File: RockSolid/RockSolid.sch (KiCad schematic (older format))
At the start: 24 parts, among them Q1 IRF540N, U1 L78L05_TO92, U2 74HC04, Y1 10 Mhz

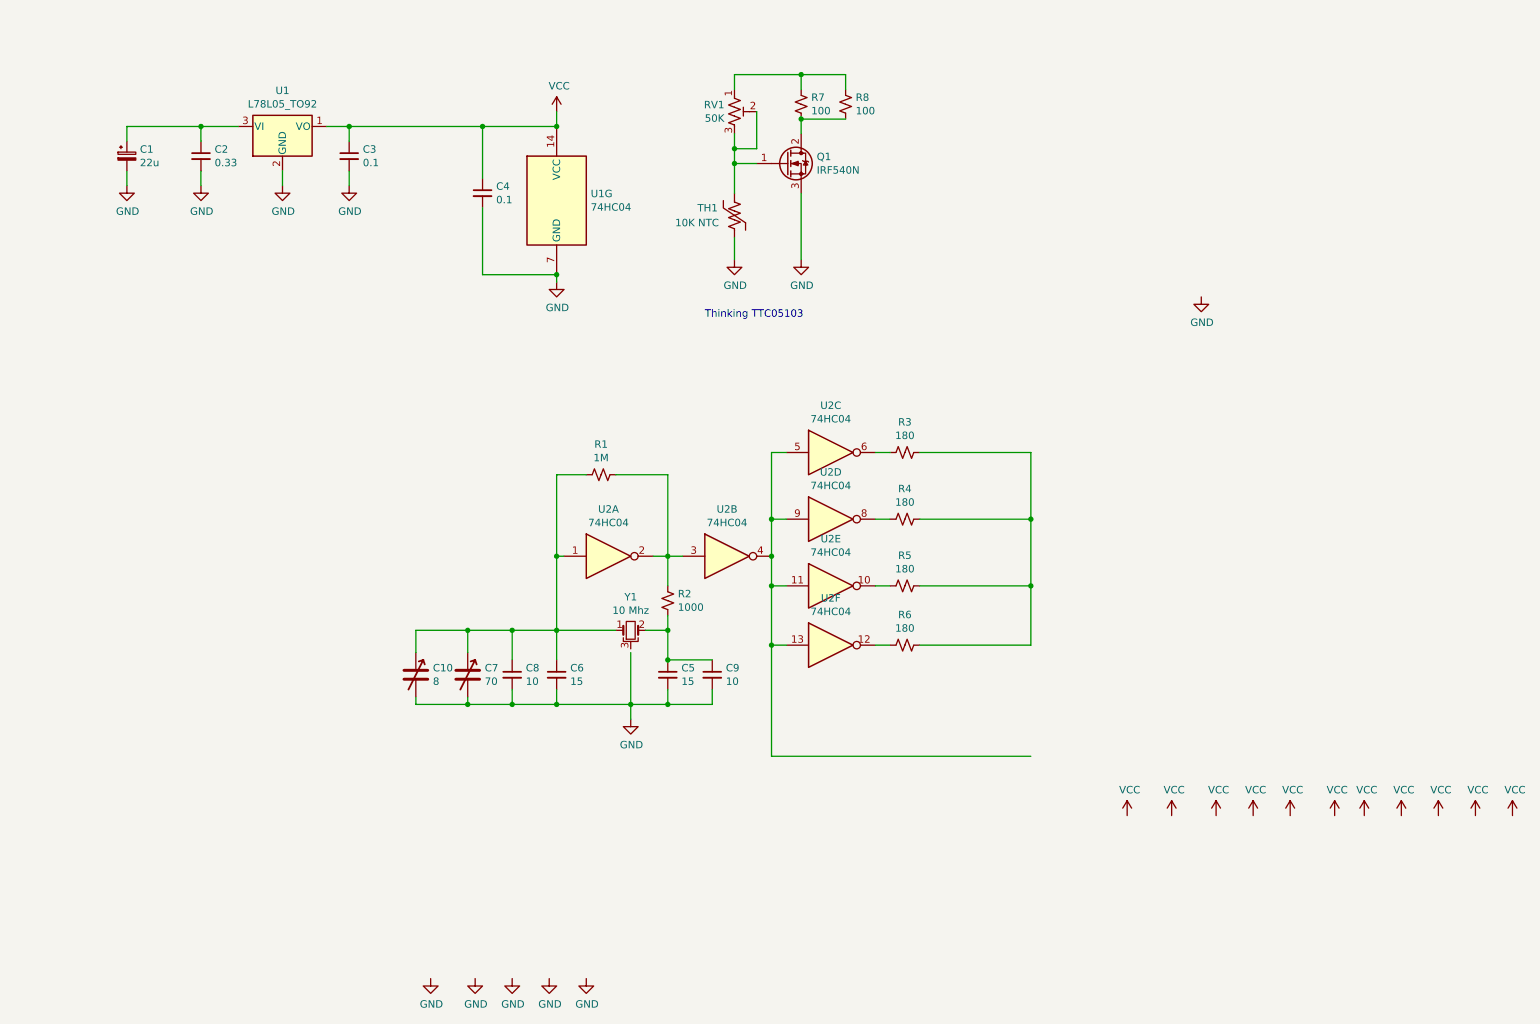
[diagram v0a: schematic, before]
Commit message: Finished schematic, initial board layout
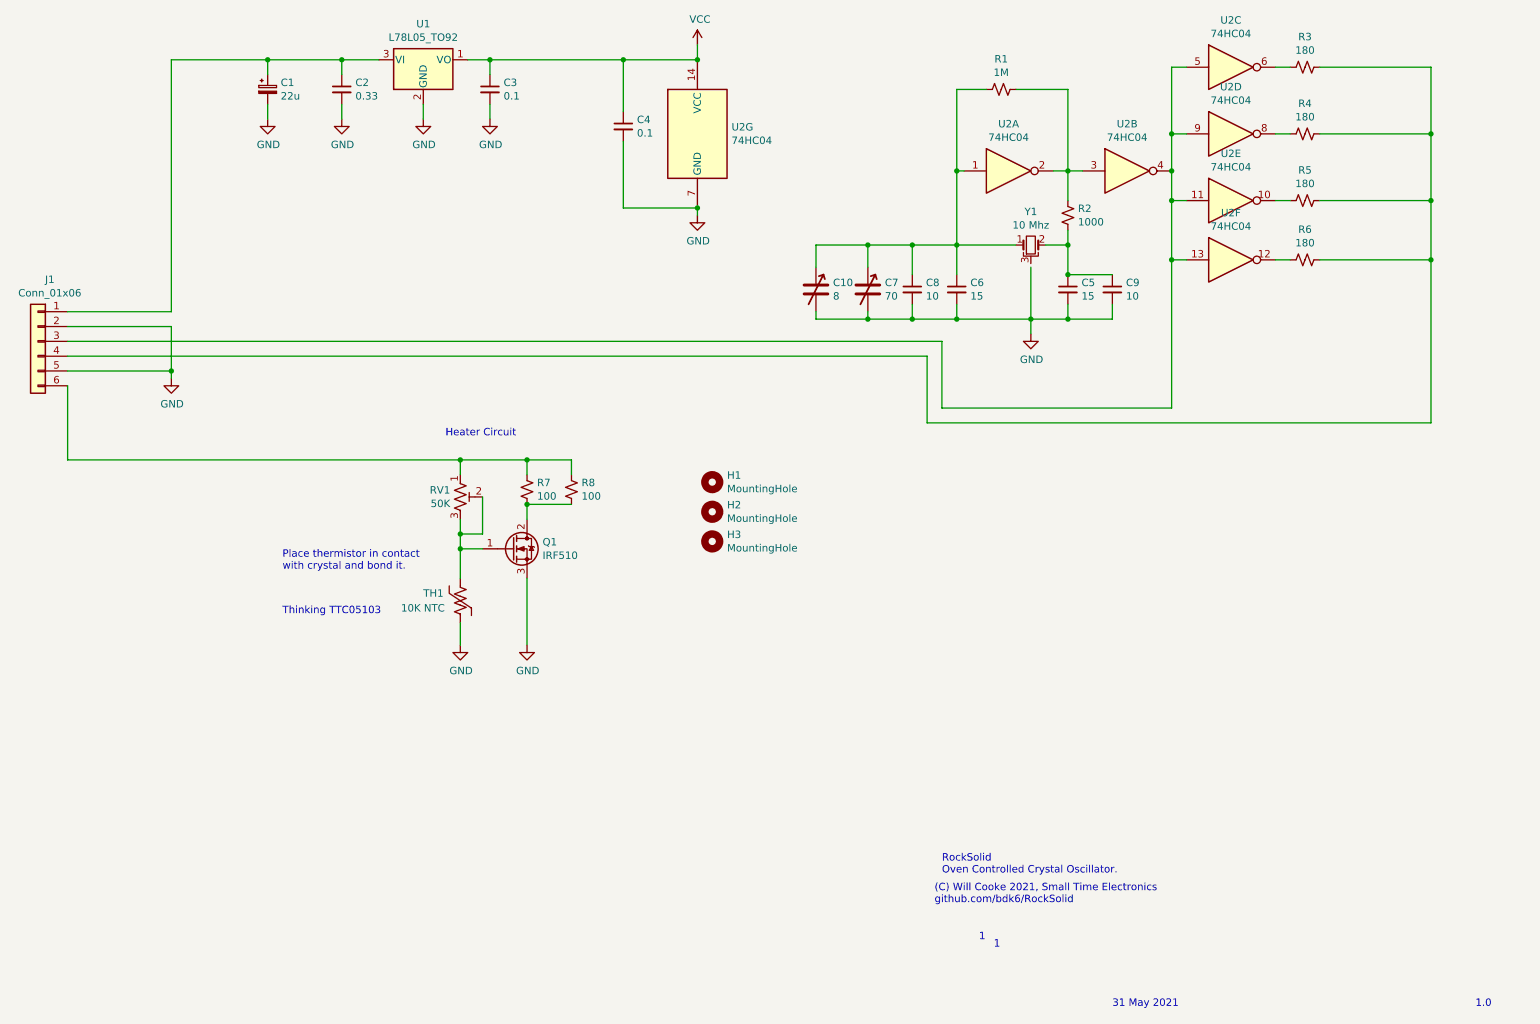
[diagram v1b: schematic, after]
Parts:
- added H1, H2, H3: MountingHole, MountingHole:MountingHole_2.5mm, symbol Mechanical:MountingHole
- added J1: Conn_01x06, Connector_PinHeader_2.54mm:PinHeader_1x06_P2.54mm_Vertical, symbol Connector_Generic:Conn_01x06
- C2, C3, C4, C5, C6, C8: footprint apacitor_THT:C_Disc_D4.7mm_W2.5mm_P5.00mm -> Capacitor_THT:C_Disc_D4.7mm_W2.5mm_P5.00mm
- Q1: value IRF540N -> IRF510
- R1, R2, R3, R4, R5, R6: footprint Resistor_THT:R_Axial_DIN0414_L11.9mm_D4.5mm_P15.24mm_Horizontal -> Resistor_THT:R_Axial_DIN0207_L6.3mm_D2.5mm_P7.62mm_Horizontal
- renumbered U1 to U2
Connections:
- net GND: now also J1.2 (Pin_2), J1.5 (Pin_5)
- net at U2.11, U2.13, U2.4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: now also J1.3 (Pin_3)
- net at R3.1, R4.1, R5.1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: now also J1.4 (Pin_4)
- net at C1.1, C2.1, U1.3 (VI): now also J1.1 (Pin_1)
- net at R7.1, R8.1, RV1.1: now also J1.6 (Pin_6)
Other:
- note added: "(C) Will Cooke 2021, Small Time Electronics\ngithub.com/bdk6/RockSolid\n"
- note added: "1"
- note added: "1.0"
- note added: "31 May 2021"
- note added: "Heater Circuit"
- note added: "Place thermistor in contact \nwith crystal and bond it."
- note added: "RockSolid \nOven Controlled Crystal Oscillator."
- moved on the sheet: C1, C10, C2, C3, C4, C5, C6, C7, C8, C9, Q1, R1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

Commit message: Version 1.0RC1 complete.
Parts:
- removed J1: Conn_01x06, Connector_PinHeader_2.54mm:PinHeader_1x06_P2.54mm_Vertical, symbol Connector_Generic:Conn_01x06
- removed R3, R4, R5, R6: 180, Resistor_THT:R_Axial_DIN0207_L6.3mm_D2.5mm_P7.62mm_Horizontal, symbol Device:R_Small_US
- added J1: Conn_01x04, Connector_PinHeader_2.54mm:PinHeader_1x04_P2.54mm_Vertical, symbol Connector_Generic:Conn_01x04
- added R10: 3K3, Resistor_THT:R_Axial_DIN0207_L6.3mm_D2.5mm_P7.62mm_Horizontal, symbol Device:R_Small_US
- added R9: 33K, Resistor_THT:R_Axial_DIN0207_L6.3mm_D2.5mm_P7.62mm_Horizontal, symbol Device:R_Small_US
- C1: footprint Capacitor_THT:CP_Radial_D8.0mm_P5.00mm -> Capacitor_THT:CP_Radial_D5.0mm_P2.00mm
- R7, R8: footprint Resistor_THT:R_Axial_DIN0414_L11.9mm_D4.5mm_P7.62mm_Vertical -> Resistor_THT:R_Axial_DIN0617_L17.0mm_D6.0mm_P7.62mm_Vertical
- RV1: value 50K -> 10K
- Y1: symbol Device:Crystal_GND3_Small -> RockSolid-rescue:Crystal_GND3_Small-Device
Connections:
- net GND: now also J1.3 (Pin_3)
- net VCC: now also R10.1
- net at U2.6: now also U2.10, U2.12, U2.8, J1.2 (Pin_2)
- net at C1.1, C2.1, U1.3 (VI): now also J1.1 (Pin_1)
- net at R7.1, R8.1: now also J1.4 (Pin_4), R9.1; no longer RV1.1
- new net: R10.2, R9.2, RV1.1
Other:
- note added: "All Resistors except R7 and R8 are 1/8 W 1%.\nC5 through C10 should be high precision, low temp coefficient.\nThermistor should be bonded to crystal package.\nR7 and R8 should be 2 W types.\nQ1, R7, R8 should be bonded to metal chassis.\nPower input should be regulated 12V, ABS MAX 14 V.\n"
- moved on the sheet: C1, C10, C2, C3, C4, C5, C6, C7, C8, C9, H1, H2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

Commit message: OK, NOW ver 1.0 RC1 complete.
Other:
- note added: "Populate either R9 or R10, not both."
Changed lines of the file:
@@
 Wire Wire Line
 	4550 4150 4850 4150
-Text Notes 3200 4550 0    50   ~ 0
+Text Notes 2900 4350 0    50   ~ 0
 Heater Circuit
 Wire Wire Line
@@
 $EndComp
 $Comp
-L power:VCC #PWR?
+L power:VCC #PWR0104
 U 1 1 6388FEEB
 P 4400 3850
-F 0 "#PWR?" H 4400 3700 50  0001 C CNN
+F 0 "#PWR0104" H 4400 3700 50  0001 C CNN
 F 1 "VCC" H 4417 4023 50  0000 C CNN
 F 2 "" H 4400 3850 50  0001 C CNN
@@
 Wire Wire Line
 	4400 4400 4400 3850
+Text Notes 5800 5000 0    50   ~ 0
+Populate either R9 or R10, not both.
 $EndSCHEMATC

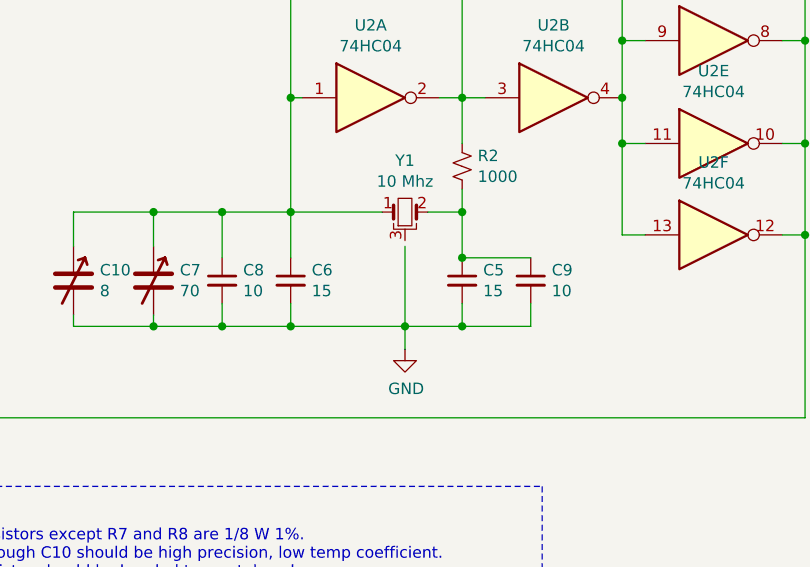
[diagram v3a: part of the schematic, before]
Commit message: v1.01 added labels on PCB, grounded crystal, silkscreen updates.
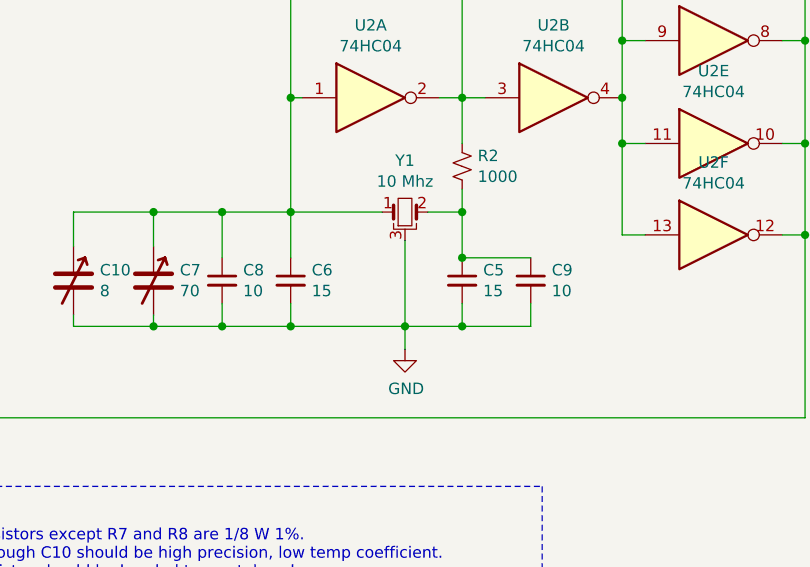
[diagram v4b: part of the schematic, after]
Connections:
- net GND: now also Y1.3
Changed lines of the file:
@@
 Connection ~ 8050 3250
-Wire Wire Line
-	7800 3200 7800 3550
 Wire Wire Line
 	8350 3450 8350 3550
@@
 Text Notes 5800 5000 0    50   ~ 0
 Populate either R9 or R10, not both.
+Wire Wire Line
+	7800 3175 7800 3550
 $EndSCHEMATC
